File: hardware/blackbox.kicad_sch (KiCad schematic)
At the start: 3 parts

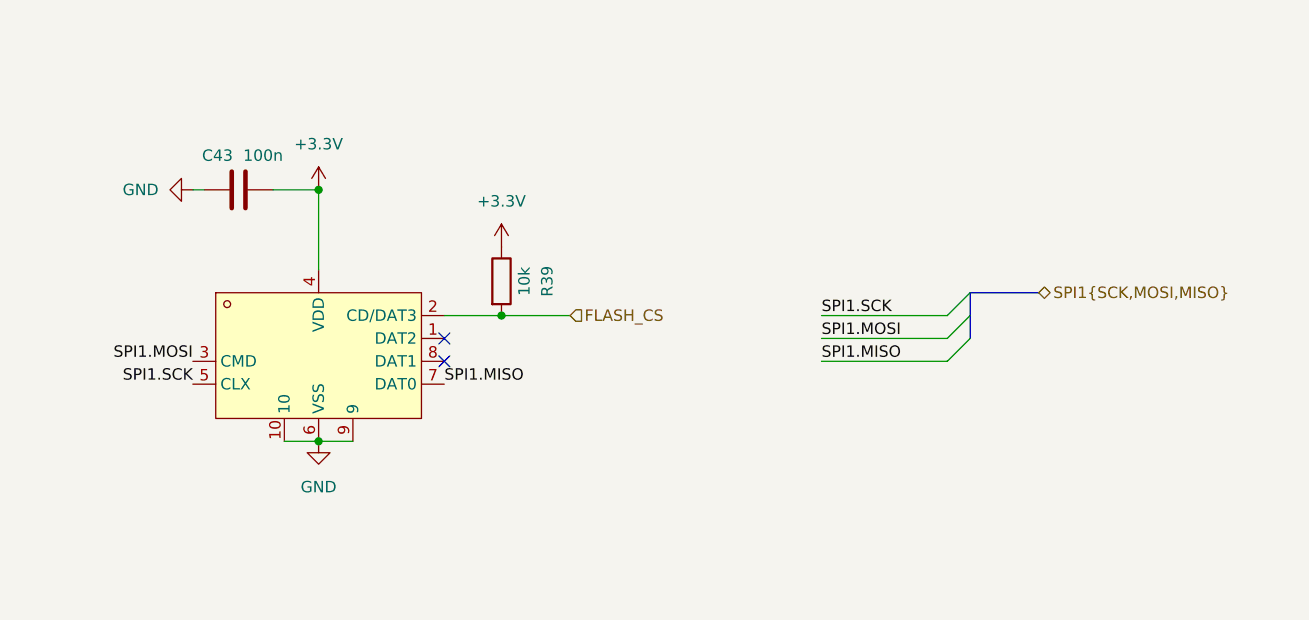
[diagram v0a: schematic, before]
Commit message: move changes from mini over to "maxi"
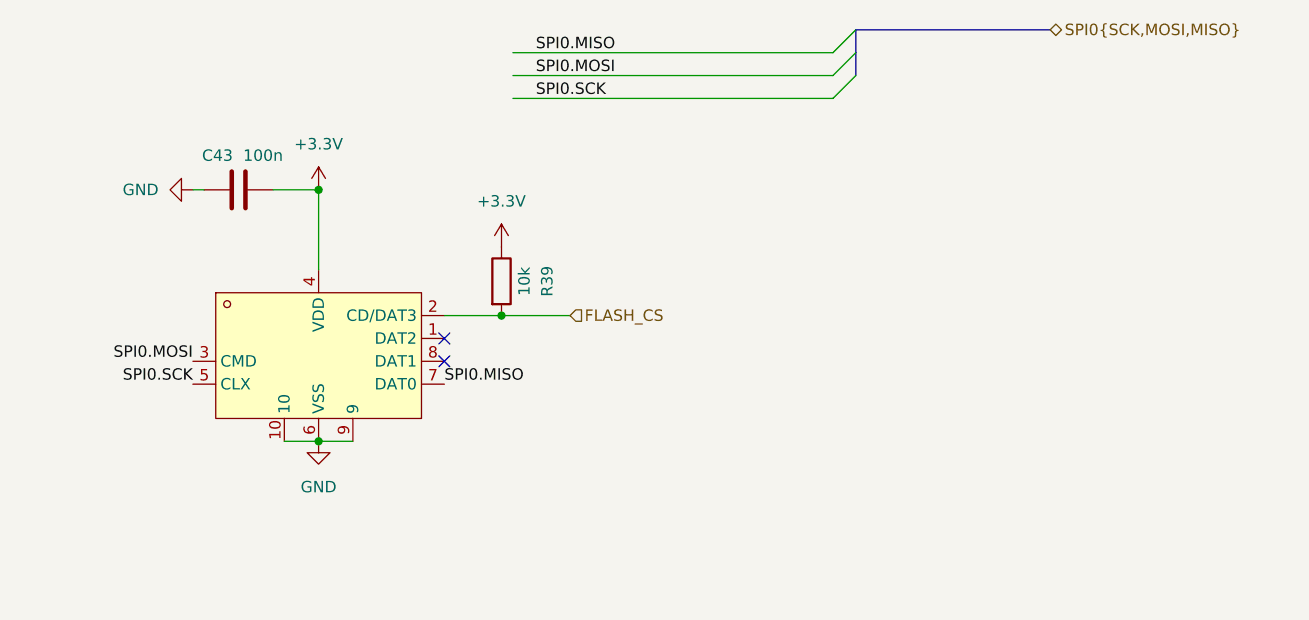
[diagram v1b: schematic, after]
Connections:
- net SPI1.MISO renamed SPI0.MISO
- net SPI1.MOSI renamed SPI0.MOSI
- net SPI1.SCK renamed SPI0.SCK
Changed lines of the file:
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@@
 	)
 	(bus_entry
-		(at 142.24 67.31)
+		(at 129.54 35.56)
 		(size 2.54 -2.54)
 		(stroke
@@
 	)
 	(bus_entry
-		(at 142.24 64.77)
+		(at 129.54 40.64)
 		(size 2.54 -2.54)
 		(stroke
@@
 	)
 	(bus_entry
-		(at 142.24 69.85)
+		(at 129.54 38.1)
 		(size 2.54 -2.54)
 		(stroke
@@
 	(bus
 		(pts
-			(xy 144.78 62.23) (xy 144.78 64.77)
-		)
-		(stroke
-			(width 0)
-			(type default)
-		)
-	)
-	(wire
-		(pts
-			(xy 128.27 69.85) (xy 142.24 69.85)
+			(xy 132.08 35.56) (xy 132.08 33.02)
+		)
+		(stroke
+			(width 0)
+			(type default)
+		)
+	)
+	(bus
+		(pts
+			(xy 132.08 33.02) (xy 153.67 33.02)
 		)
 		(stroke
@@
 		)
 	)
+	(wire
+		(pts
+			(xy 93.98 40.64) (xy 129.54 40.64)
+		)
+		(stroke
+			(width 0)
+			(type default)
+		)
+	)
 	(bus
 		(pts
-			(xy 144.78 64.77) (xy 144.78 67.31)
-		)
-		(stroke
-			(width 0)
-			(type default)
-		)
-	)
-	(wire
-		(pts
-			(xy 128.27 64.77) (xy 142.24 64.77)
+			(xy 132.08 38.1) (xy 132.08 35.56)
 		)
 		(stroke
@@
 	(wire
 		(pts
-			(xy 128.27 67.31) (xy 142.24 67.31)
-		)
-		(stroke
-			(width 0)
-			(type default)
-		)
-	)
-	(wire
-		(pts
 			(xy 59.69 50.8) (xy 58.42 50.8)
 		)
@@
 		)
 	)
-	(bus
-		(pts
-			(xy 152.4 62.23) (xy 144.78 62.23)
+	(wire
+		(pts
+			(xy 93.98 35.56) (xy 129.54 35.56)
+		)
+		(stroke
+			(width 0)
+			(type default)
+		)
+	)
+	(wire
+		(pts
+			(xy 93.98 38.1) (xy 129.54 38.1)
 		)
 		(stroke
@@
 		)
 	)
-	(label "SPI1.SCK"
+	(label "SPI0.MISO"
+		(at 96.52 35.56 0)
+		(effects
+			(font
+				(size 1.27 1.27)
+			)
+			(justify left bottom)
+		)
+	)
+	(label "SPI0.MOSI"
+		(at 96.52 38.1 0)
+		(effects
+			(font
+				(size 1.27 1.27)
+			)
+			(justify left bottom)
+		)
+	)
+	(label "SPI0.SCK"
 		(at 58.42 72.39 180)
 		(effects
@@
 		)
 	)
-	(label "SPI1.MISO"
-		(at 128.27 69.85 0)
-		(effects
-			(font
-				(size 1.27 1.27)
-			)
-			(justify left bottom)
-		)
-	)
-	(label "SPI1.MISO"
+	(label "SPI0.SCK"
+		(at 96.52 40.64 0)
+		(effects
+			(font
+				(size 1.27 1.27)
+			)
+			(justify left bottom)
+		)
+	)
+	(label "SPI0.MISO"
 		(at 86.36 72.39 0)
 		(effects
@@
 		)
 	)
-	(label "SPI1.MOSI"
-		(at 128.27 67.31 0)
-		(effects
-			(font
-				(size 1.27 1.27)
-			)
-			(justify left bottom)
-		)
-	)
-	(label "SPI1.SCK"
-		(at 128.27 64.77 0)
-		(effects
-			(font
-				(size 1.27 1.27)
-			)
-			(justify left bottom)
-		)
-	)
-	(label "SPI1.MOSI"
+	(label "SPI0.MOSI"
 		(at 58.42 69.85 180)
 		(effects
@@
 		)
 	)
-	(hierarchical_label "SPI1{SCK,MOSI,MISO}"
+	(hierarchical_label "SPI0{SCK,MOSI,MISO}"
 		(shape bidirectional)
-		(at 152.4 62.23 0)
-		(effects
-			(font
+		(at 153.67 33.02 0)
+		(effects
+			(font

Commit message: rev2 update
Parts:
- removed C43: 100n, Capacitor_SMD:C_0201_0603Metric, symbol Device:C
- removed Card1: TF-021B-H265, lib:TF-SMD_TF-021B-H265, symbol lib:TF-021B-H265
- removed R39: 10k, Resistor_SMD:R_0201_0603Metric, symbol Device:R
- added C44: 100n, Capacitor_SMD:C_0201_0603Metric, symbol Device:C
- added Card2: TF PUSH, lib:TF-SMD_TF-PUSH, symbol lib:TFPUSH
- added R54: 10k, Resistor_SMD:R_0201_0603Metric, symbol Device:R
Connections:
- net +3.3V: now also C44.1, Card2.4 (VDD), R54.1
- net FLASH_CS: now also Card2.2 (CD/DAT3), R54.2
- net GND: now also C44.2, Card2.10, Card2.11, Card2.12, Card2.13, Card2.6 (VSS)
- new net SPI1.MISO: Card2.7 (DAT0)
- new net SPI1.MOSI: Card2.3 (CMD)
- new net SPI1.SCK: Card2.5 (CLX)
- no-connect marks 2 -> 3

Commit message: lite done
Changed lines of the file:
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@@
-	(symbol
-		(lib_id "power:GND")
-		(at 93.98 72.39 0)
-		(unit 1)
-		(body_style 1)
-		(exclude_from_sim no)
-		(in_bom yes)
-		(on_board yes)
-		(in_pos_files yes)
-		(dnp no)
-		(fields_autoplaced yes)
-		(property "Reference" "#PWR062"
-			(at 93.98 78.74 0)
-			(hide yes)
-			(show_name no)
-			(do_not_autoplace no)
-			(effects
-				(font
-					(size 1.27 1.27)
-				)
-			)
-		)
-		(property "Value" "GND"
-			(at 93.9799 76.2 90)
-			(show_name no)
-			(do_not_autoplace no)
-			(effects
-				(font
-					(size 1.27 1.27)
-				)
-				(justify right)
-			)
-		)
-		(property "Footprint" ""
-			(at 93.98 72.39 0)
-			(hide yes)
-			(show_name no)
-			(do_not_autoplace no)
-			(effects
-				(font
-					(size 1.27 1.27)
-				)
-			)
-		)
-		(property "Datasheet" ""
-			(at 93.98 72.39 0)
-			(hide yes)
-			(show_name no)
-			(do_not_autoplace no)
-			(effects
-				(font
-					(size 1.27 1.27)
-				)
-			)
-		)
-		(property "Description" "Power symbol creates a global label with name \"GND\" , ground"
-			(at 93.98 72.39 0)
-			(hide yes)
-			(show_name no)
-			(do_not_autoplace no)
-			(effects
-				(font
-					(size 1.27 1.27)
-				)
-			)
-		)
-		(pin "1"
-		)
-		(instances
-			(project "OpenFC"
-				(path "/fb88b6f9-ee39-4640-a9d4-04a17ceeac64/4c4f8c63-c695-4758-b1bc-c8af53273c68"
-					(reference "#PWR062")
-					(unit 1)
-				)
-			)
-		)
-	)
 	(symbol
 		(lib_id "power:GND")
@@
 	)
 	(symbol
+		(lib_id "power:GND")
+		(at 93.98 72.39 0)
+		(unit 1)
+		(body_style 1)
+		(exclude_from_sim no)
+		(in_bom yes)
+		(on_board yes)
+		(in_pos_files yes)
+		(dnp no)
+		(fields_autoplaced yes)
+		(property "Reference" "#PWR07"
+			(at 93.98 78.74 0)
+			(hide yes)
+			(show_name no)
+			(do_not_autoplace no)
+			(effects
+				(font
+					(size 1.27 1.27)
+				)
+			)
+		)
+		(property "Value" "GND"
+			(at 93.98 77.47 0)
+			(show_name no)
+			(do_not_autoplace no)
+			(effects
+				(font
+					(size 1.27 1.27)
+				)
+			)
+		)
+		(property "Footprint" ""
+			(at 93.98 72.39 0)
+			(hide yes)
+			(show_name no)
+			(do_not_autoplace no)
+			(effects
+				(font
+					(size 1.27 1.27)
+				)
+			)
+		)
+		(property "Datasheet" ""
+			(at 93.98 72.39 0)
+			(hide yes)
+			(show_name no)
+			(do_not_autoplace no)
+			(effects
+				(font
+					(size 1.27 1.27)
+				)
+			)
+		)
+		(property "Description" "Power symbol creates a global label with name \"GND\" , ground"
+			(at 93.98 72.39 0)
+			(hide yes)
+			(show_name no)
+			(do_not_autoplace no)
+			(effects
+				(font
+					(size 1.27 1.27)
+				)
+			)
+		)
+		(pin "1"
+		)
+		(instances
+			(project "OpenFC"
+				(path "/fb88b6f9-ee39-4640-a9d4-04a17ceeac64/4c4f8c63-c695-4758-b1bc-c8af53273c68"
+					(reference "#PWR07")
+					(unit 1)
+				)
+			)
+		)
+	)
+	(symbol
 		(lib_id "Device:C")
 		(at 93.98 67.31 0)
@@
 		)
 	)
-	(embedded_fonts no)
 )

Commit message: routing
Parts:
- renumbered C44 to C35, Card2 to Card1, R54 to R30
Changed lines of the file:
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@@
 		(in_pos_files yes)
 		(dnp no)
-		(property "Reference" "R54"
+		(property "Reference" "R30"
 			(at 107.95 78.74 90)
 			(show_name no)
@@
 			(project "OpenFC"
 				(path "/fb88b6f9-ee39-4640-a9d4-04a17ceeac64/4c4f8c63-c695-4758-b1bc-c8af53273c68"
-					(reference "R54")
+					(reference "R30")
 					(unit 1)
 				)
@@
 		(in_pos_files yes)
 		(dnp no)
-		(property "Reference" "#PWR0164"
+		(property "Reference" "#PWR0128"
 			(at 78.74 72.39 0)
 			(hide yes)
@@
 			(project "OpenFC"
 				(path "/fb88b6f9-ee39-4640-a9d4-04a17ceeac64/4c4f8c63-c695-4758-b1bc-c8af53273c68"
-					(reference "#PWR0164")
+					(reference "#PWR0128")
 					(unit 1)
 				)
@@
 		(dnp no)
 		(fields_autoplaced yes)
-		(property "Reference" "#PWR0159"
+		(property "Reference" "#PWR0129"
 			(at 93.98 64.77 0)
 			(hide yes)
@@
 			(project "OpenFC"
 				(path "/fb88b6f9-ee39-4640-a9d4-04a17ceeac64/4c4f8c63-c695-4758-b1bc-c8af53273c68"
-					(reference "#PWR0159")
+					(reference "#PWR0129")
 					(unit 1)
 				)
@@
 		(dnp no)
 		(fields_autoplaced yes)
-		(property "Reference" "Card2"
+		(property "Reference" "Card1"
 			(at 48.26 73.6599 0)
 			(show_name no)
@@
 			(project "OpenFC"
 				(path "/fb88b6f9-ee39-4640-a9d4-04a17ceeac64/4c4f8c63-c695-4758-b1bc-c8af53273c68"
-					(reference "Card2")
+					(reference "Card1")
 					(unit 1)
 				)
@@
 		(dnp no)
 		(fields_autoplaced yes)
-		(property "Reference" "#PWR0163"
+		(property "Reference" "#PWR0127"
 			(at 57.15 96.52 0)
 			(hide yes)
@@
 			(project "OpenFC"
 				(path "/fb88b6f9-ee39-4640-a9d4-04a17ceeac64/4c4f8c63-c695-4758-b1bc-c8af53273c68"
-					(reference "#PWR0163")
+					(reference "#PWR0127")
 					(unit 1)
 				)
@@
 		(dnp no)
 		(fields_autoplaced yes)
-		(property "Reference" "#PWR0162"
+		(property "Reference" "#PWR0125"
 			(at 52.07 96.52 0)
 			(hide yes)
@@
 			(project "OpenFC"
 				(path "/fb88b6f9-ee39-4640-a9d4-04a17ceeac64/4c4f8c63-c695-4758-b1bc-c8af53273c68"
-					(reference "#PWR0162")
+					(reference "#PWR0125")
 					(unit 1)
 				)
@@
 		(dnp no)
 		(fields_autoplaced yes)
-		(property "Reference" "#PWR0161"
+		(property "Reference" "#PWR0126"
 			(at 57.15 53.34 0)
 			(hide yes)
@@
 			(project "OpenFC"
 				(path "/fb88b6f9-ee39-4640-a9d4-04a17ceeac64/4c4f8c63-c695-4758-b1bc-c8af53273c68"
-					(reference "#PWR0161")
+					(reference "#PWR0126")
 					(unit 1)
 				)
@@
 		(dnp no)
 		(fields_autoplaced yes)
-		(property "Reference" "#PWR07"
+		(property "Reference" "#PWR0130"
 			(at 93.98 78.74 0)
 			(hide yes)
@@
 			(project "OpenFC"
 				(path "/fb88b6f9-ee39-4640-a9d4-04a17ceeac64/4c4f8c63-c695-4758-b1bc-c8af53273c68"
-					(reference "#PWR07")
+					(reference "#PWR0130")
 					(unit 1)
 				)
@@
 		(in_pos_files yes)
 		(dnp no)
-		(property "Reference" "C44"
+		(property "Reference" "C35"
 			(at 97.536 68.834 0)
 			(show_name no)
@@
 			(project "OpenFC"
 				(path "/fb88b6f9-ee39-4640-a9d4-04a17ceeac64/4c4f8c63-c695-4758-b1bc-c8af53273c68"
-					(reference "C44")
+					(reference "C35")
 					(unit 1)
 				)
@@
 		(dnp no)
 		(fields_autoplaced yes)
-		(property "Reference" "#PWR0160"
+		(property "Reference" "#PWR0124"
 			(at 52.07 53.34 0)
 			(hide yes)
@@
 			(project "OpenFC"
 				(path "/fb88b6f9-ee39-4640-a9d4-04a17ceeac64/4c4f8c63-c695-4758-b1bc-c8af53273c68"
-					(reference "#PWR0160")
+					(reference "#PWR0124")
 					(unit 1)
 				)
@@
 		)
 	)
+	(embedded_fonts no)
 )
